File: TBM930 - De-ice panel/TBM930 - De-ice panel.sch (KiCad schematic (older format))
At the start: 21 parts, among them J1 Conn_01x02_Male, J2 Conn_01x02_Male, J3 Conn_01x02_Male, J4 Conn_01x02_Male, J5 Conn_01x02_Male, J6 Conn_01x02_Male, J7 Conn_01x02_Male, Q1 BS170, Q2 BS170, U1 ArduinoMEGA2560PROEmbed

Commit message: TBM930 updates
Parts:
- removed J1, J2, J3, J4, J5, J6, J7: Conn_01x02_Male, symbol Connector:Conn_01x02_Male
- added Q3: BS170, Package_TO_SOT_THT:TO-92_Inline, symbol Transistor_FET:BS170
- added R4: 10k, Resistor_SMD:R_1206_3216Metric_Pad1.30x1.75mm_HandSolder, symbol Device:R
- added SW1, SW2, SW3, SW4, SW5, SW6, SW7: SW_SPDT, Switches:MiniToggleSPDT terminal mount, symbol Switch:SW_SPDT
- D1, D2, D3, D4, D5: footprint (none) -> LED_THT:LED_D5.0mm
- D6, D7, D8: footprint (none) -> LED_SMD:LED_1206_3216Metric_Pad1.42x1.75mm_HandSolder
- R1, R2, R3: footprint (none) -> Resistor_SMD:R_1206_3216Metric_Pad1.30x1.75mm_HandSolder
- U1: footprint (none) -> Ardino:MEGA2560PROEmbed
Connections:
- net labels added: ANC_GND, LED_MASTER_GND, MASTER_POWER
- net labels removed: LED_GND
- wire segments 19 -> 37
- no-connect marks 62 -> 68
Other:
- note added: "Annunciators"
- note added: "Backlight"
- note added: "LED brightness control"
- note added: "Master LED power"
- note removed: "Annunciator LED brightness control"
- note removed: "Backlight LED brightness control"
- moved on the sheet: D1, D2, D3, D4, D5, D6, D7, D8, R1, R2, R3

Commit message: Switch to use the LED driver chip
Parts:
- removed D6, D7, D8: LED, LED_SMD:LED_1206_3216Metric_Pad1.42x1.75mm_HandSolder, symbol Device:LED
- removed Q1, Q2, Q3: BS170, Package_TO_SOT_THT:TO-92_Inline, symbol Transistor_FET:BS170
- removed SW1, SW2, SW3, SW4, SW5, SW6, SW7: SW_SPDT, Switches:MiniToggleSPDT terminal mount, symbol Switch:SW_SPDT
- added C1: 0.1uF, Capacitor_THT:C_Disc_D5.0mm_W2.5mm_P5.00mm, symbol Device:C
- added J1: SW_AIRFRAME_DE_ICE, Connector_Molex:Molex_KK-254_AE-6410-02A_1x02_P2.54mm_Vertical, symbol Connector:Conn_01x02_Male
- added J2: SW_ICE_LIGHT, Connector_Molex:Molex_KK-254_AE-6410-02A_1x02_P2.54mm_Vertical, symbol Connector:Conn_01x02_Male
- added J3: SW_PROP_DE_ICE, Connector_Molex:Molex_KK-254_AE-6410-02A_1x02_P2.54mm_Vertical, symbol Connector:Conn_01x02_Male
- added J4: SW_WIND_SHIELD, Connector_Molex:Molex_KK-254_AE-6410-02A_1x02_P2.54mm_Vertical, symbol Connector:Conn_01x02_Male
- added J5: SW_PITOT_L_HTR, Connector_Molex:Molex_KK-254_AE-6410-02A_1x02_P2.54mm_Vertical, symbol Connector:Conn_01x02_Male
- added J6: SW_PITOT_R_HTR, Connector_Molex:Molex_KK-254_AE-6410-02A_1x02_P2.54mm_Vertical, symbol Connector:Conn_01x02_Male
- added J7: SW_INERT_SEP, Connector_Molex:Molex_KK-254_AE-6410-02A_1x02_P2.54mm_Vertical, symbol Connector:Conn_01x02_Male
- added U2: TLC5916IN, Package_DIP:DIP-16_W7.62mm_Socket, symbol Mobiflight~docs:TLC5916IN
- D4: value WINDSHILED 1 -> WINDSHIELD 1
- R1: footprint Resistor_SMD:R_1206_3216Metric_Pad1.30x1.75mm_HandSolder -> Resistor_THT:R_Axial_DIN0207_L6.3mm_D2.5mm_P7.62mm_Horizontal
- R2, R3, R4: value 10k -> R; footprint Resistor_SMD:R_1206_3216Metric_Pad1.30x1.75mm_HandSolder -> Resistor_THT:R_Axial_DIN0207_L6.3mm_D2.5mm_P7.62mm_Horizontal
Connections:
- net labels added: +5V_LED, AIRFRAME_1, AIRFRAME_2, ANNUNCIATOR_CLOCK, ANNUNCIATOR_DATA, ANNUNCIATOR_LATCH, CURRENT_LIMITER, PROP, WINDSHIELD_1, WINDSHIELD_2
- net labels removed: AIRFRAME_1_LED, AIRFRAME_2_LED, ANC_GND, BACKLIGHT_BRIGHTNESS, BACKLIGHT_GND, LED_MASTER_GND, MASTER_POWER, PROP_LED, WINDSHIELD_1_LED, WINDSHIELD_2_LED
- wire segments 37 -> 23
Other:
- note added: "Switches are mounted to the board via the shaft\nand connected with Molex connectors so they can\nbe removed and re-used in other projects.\n"
- note removed: "Annunciators"
- note removed: "Backlight"
- note removed: "Backlight LEDs"
- note removed: "LED brightness control"
- note removed: "Master LED power"
- moved on the sheet: D1, D2, D3, D4, D5

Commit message: Create global library for footprints and symbols
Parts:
- removed R4: R, Resistor_THT:R_Axial_DIN0207_L6.3mm_D2.5mm_P7.62mm_Horizontal, symbol Device:R
- removed U1: ArduinoMEGA2560PROEmbed, Ardino:MEGA2560PROEmbed, symbol Arduino:ArduinoMEGA2560PROEmbed
- removed U2: TLC5916IN, Package_DIP:DIP-16_W7.62mm_Socket, symbol Mobiflight~docs:TLC5916IN
- added C2: 0.1uF, Capacitor_THT:C_Disc_D5.0mm_W2.5mm_P5.00mm, symbol Device:C
- added D10, D11, D12, D13, D14, D15, D16, D17, D18, D19, D20, D6, D7, D8, D9: LED, LED_SMD:LED_1206_3216Metric_Pad1.42x1.75mm_HandSolder, symbol Device:LED
- added J8: Barrel_Jack, Global MobiFlight panel parts:BarrelJack_Horizontal, symbol Connector:Barrel_Jack
- added SW1: SW_Push_Dual, symbol Switch:SW_Push_Dual
- added U1, U2: TLC5917IN, Package_DIP:DIP-16_W7.62mm, symbol Global_MobiFlight_panel_parts:TLC5917IN
- added U3: ArduinoMEGA2560PROEmbed, Ardino:MEGA2560PROEmbed, symbol Global_MobiFlight_panel_parts:ArduinoMEGA2560PROEmbed
- R2, R3: value R -> 1k
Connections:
- net labels added: +12V_LED, BACKLIGHT1, BACKLIGHT2, BACKLIGHT3, BACKLIGHT4, BACKLIGHT5, BACKLIGHT_BRIGHTNESS, BACKLIGHT_CLOCK, BACKLIGHT_DATA, BACKLIGHT_LATCH, LTS_TEST
- net labels removed: CURRENT_LIMITER
- wire segments 23 -> 35
- no-connect marks 68 -> 69
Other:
- note added: "12V LED power"
- note added: "Backlight LEDs"
- note added: "Light test"
- moved on the sheet: C1, D1, D2, D3, D4, D5, J1, J2, J3, J4, J5, J6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

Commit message: Massive de-ice panel update
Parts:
- removed D15: LED, LED_SMD:LED_1206_3216Metric_Pad1.42x1.75mm_HandSolder, symbol Device:LED
- removed SW1: SW_Push_Dual, symbol Switch:SW_Push_Dual
- removed U2: TLC5917IN, Package_DIP:DIP-16_W7.62mm, symbol Global_MobiFlight_panel_parts:TLC5917IN
- added D20, D21, D22: LED, LED_SMD:LED_1206_3216Metric_Pad1.42x1.75mm_HandSolder, symbol Device:LED
- added SW1: SW_Push, Button_Switch_THT:SW_PUSH_6mm_H9.5mm, symbol Switch:SW_Push
- added U3: TLC5917IN, Package_DIP:DIP-16_W7.62mm, symbol Global_MobiFlight_panel_parts:TLC5917IN
- U1: renamed from U3; footprint Ardino:MEGA2560PROEmbed -> Global MobiFlight panel parts:MEGA2560PROEmbed
- renumbered D16 to D15, D17 to D16, D18 to D17, D19 to D18, D20 to D19, U1 to U2
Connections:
- net labels added: BACKLIGHT6, LED_CLOCK, LED_DATA, LED_LATCH
- net labels removed: ANNUNCIATOR_CLOCK, ANNUNCIATOR_DATA, ANNUNCIATOR_LATCH, BACKLIGHT_CLOCK, BACKLIGHT_DATA, BACKLIGHT_LATCH
- wire segments 35 -> 32
- no-connect marks 69 -> 68
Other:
- moved on the sheet: D14, J8, R2

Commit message: Routed!
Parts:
- added D23, D24: LED, LED_SMD:LED_1206_3216Metric_Pad1.42x1.75mm_HandSolder, symbol Device:LED
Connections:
- net labels added: BACKLIGHT7
- wire segments 32 -> 34
- no-connect marks 68 -> 67
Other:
- moved on the sheet: C1, C2, D1, D10, D11, D12, D13, D14, D15, D16, D17, D18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

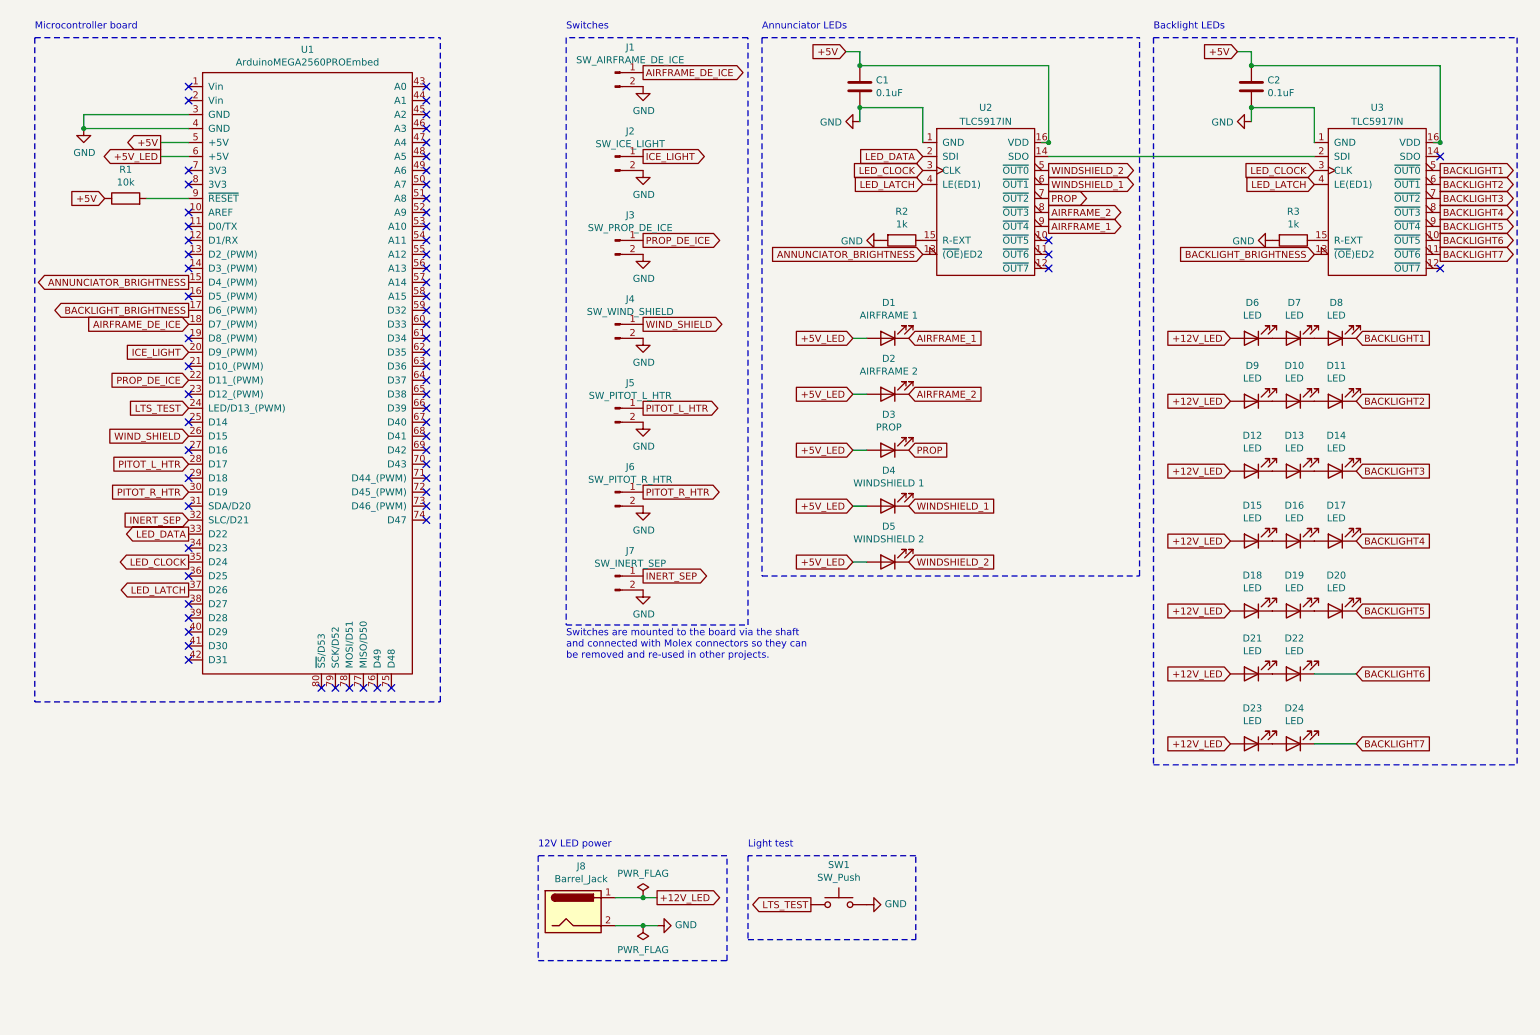
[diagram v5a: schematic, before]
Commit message: Switch to smaller Arduino
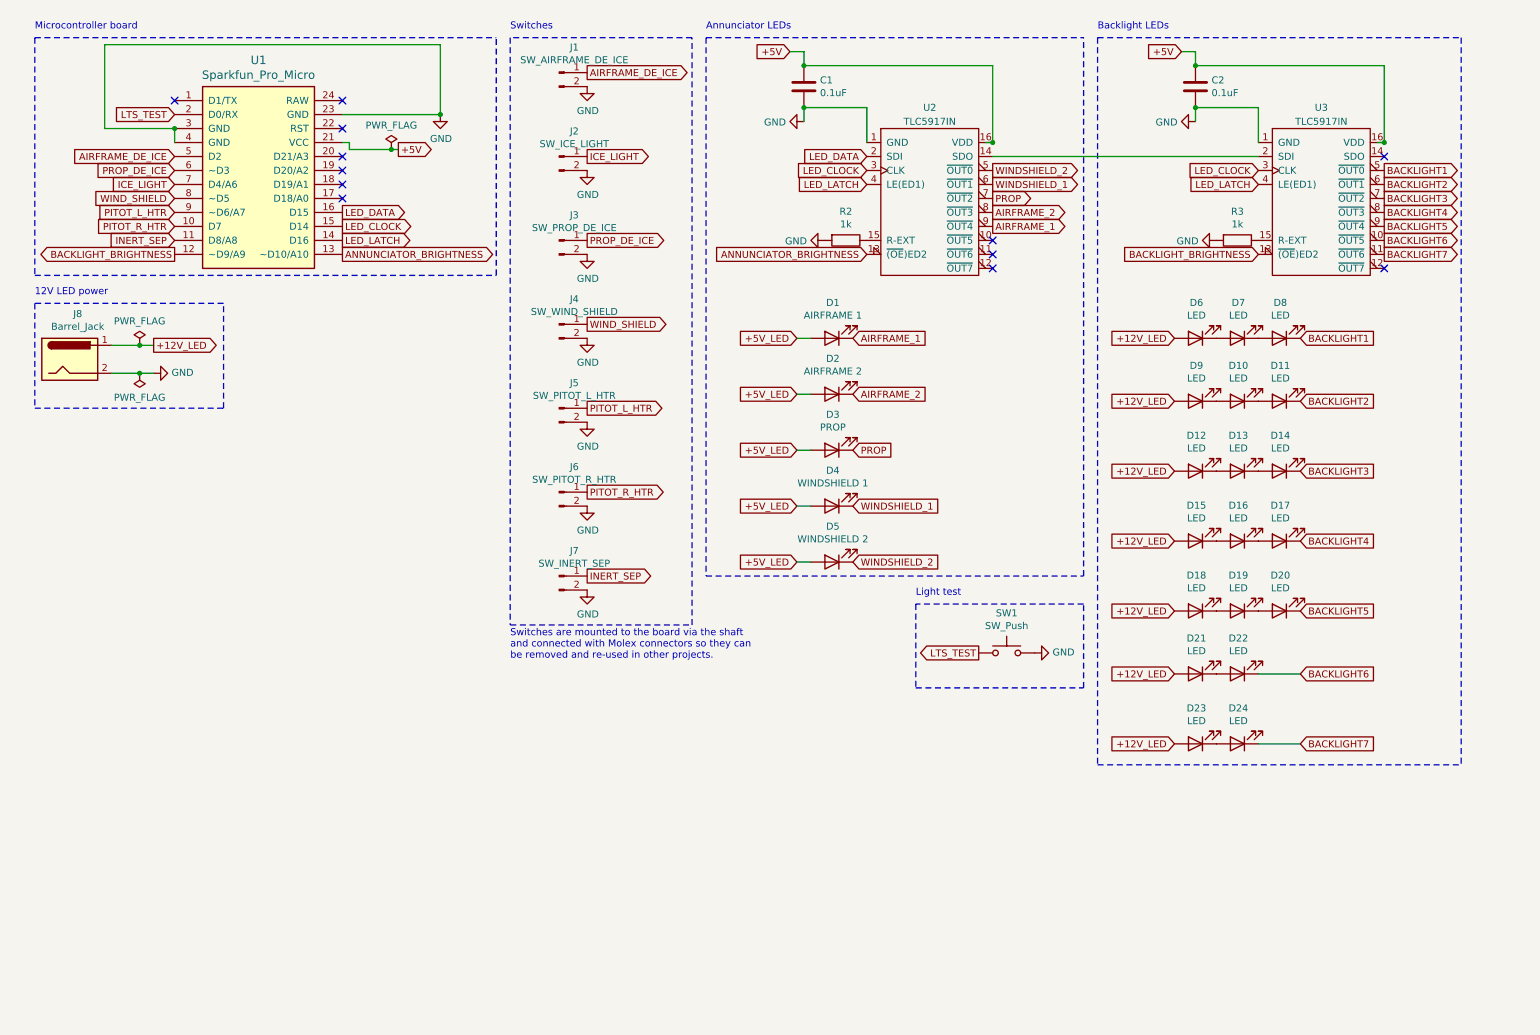
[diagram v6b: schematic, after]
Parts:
- removed R1: 10k, Resistor_THT:R_Axial_DIN0207_L6.3mm_D2.5mm_P7.62mm_Horizontal, symbol Device:R
- removed U1: ArduinoMEGA2560PROEmbed, Global MobiFlight panel parts:MEGA2560PROEmbed, symbol Global_MobiFlight_panel_parts:ArduinoMEGA2560PROEmbed
- added U1: Sparkfun_Pro_Micro, Arduino:Sparkfun_Pro_Micro, symbol Arduino:Sparkfun_Pro_Micro
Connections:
- wire segments 34 -> 38
- no-connect marks 67 -> 12
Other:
- moved on the sheet: C1, C2, D1, D10, D11, D12, D13, D14, D15, D16, D17, D18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

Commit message: Microcontroller righton the board
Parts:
- removed U1: Sparkfun_Pro_Micro, Arduino:Sparkfun_Pro_Micro, symbol Arduino:Sparkfun_Pro_Micro
- added C10, C9: 20pF, symbol Device:C
- added C11, C14, C8: 0.1uF, symbol Device:C
- added C12, C6: 10uF, symbol Device:CP
- added C13, C3, C4, C5, C7: 1uF, symbol Device:C
- added D25, D27, D28: LED, symbol Device:LED
- added FB1: 500mA, symbol Device:Ferrite_Bead
- added FB2: Ferrite_Bead, symbol Device:Ferrite_Bead
- added J10: AVR-ISP-6, symbol Connector:AVR-ISP-6
- added J9: USB_B_Micro, symbol Connector:USB_B_Micro
- added NT1: Net-Tie_2, symbol Device:Net-Tie_2
- added R1, R4: 330, symbol Device:R
- added R5: 1K, symbol Device:R
- added R6, R7: 22, symbol Device:R
- added R8: 10K, symbol Device:R
- added SW2: SW_Push, symbol Switch:SW_Push
- added U1: ATmega16U4-MU-Exposed-Extra-Pins, Package_DFN_QFN:QFN-44-1EP_7x7mm_P0.5mm_EP5.2x5.2mm, symbol Global_MobiFlight_panel_parts:ATmega16U4-MU-Exposed-Extra-Pins
- added Y1: 16MHz, symbol Device:Crystal
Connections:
- net labels added: A0, A1, A2, A3, A4, A5, BACKLIGHT_BRIGHT, D+, D-, D10, D12, D13, D17, D2, D3, D4, D5, D6, D7, D8, D9, INDICATOR_BRIGHT, MISO, MOSI, RXI, SCK, TXO, XTAL1, XTAL2, ~RESET
- net labels removed: +5V_LED, ANNUNCIATOR_BRIGHTNESS, BACKLIGHT_BRIGHTNESS
- wire segments 38 -> 115
- no-connect marks 12 -> 13
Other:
- note added: "AVR-ISP programing interface"
- note added: "Microcontroller"
- note added: "Oscillator"
- note added: "USB and +5V power"
- note removed: "Microcontroller board"
- moved on the sheet: C1, C2, D1, D10, D11, D12, D13, D14, D15, D16, D17, D18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

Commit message: Placed components on PCB, working on routing
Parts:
- removed FB1: 500mA, symbol Device:Ferrite_Bead
- C1: renamed from C3; footprint (none) -> Capacitor_SMD:C_0603_1608Metric; JLC (none) -> 0603; LCSC (none) -> C15849
- C10: renamed from C12; footprint (none) -> Capacitor_SMD:C_0603_1608Metric; JLC (none) -> 0603; LCSC (none) -> C15850
- C11: renamed from C13; footprint (none) -> Capacitor_SMD:C_0603_1608Metric; JLC (none) -> 0603; LCSC (none) -> C15849
- C12: renamed from C14; footprint (none) -> Capacitor_SMD:C_0603_1608Metric; JLC (none) -> 0603; LCSC (none) -> C14663
- C13: renamed from C1; footprint Capacitor_THT:C_Disc_D5.0mm_W2.5mm_P5.00mm -> Capacitor_SMD:C_0603_1608Metric; JLC (none) -> 0603; LCSC (none) -> C14663
- C14: renamed from C2; footprint Capacitor_THT:C_Disc_D5.0mm_W2.5mm_P5.00mm -> Capacitor_SMD:C_0603_1608Metric; JLC (none) -> 0603; LCSC (none) -> C14663
- C2: renamed from C4; footprint (none) -> Capacitor_SMD:C_0603_1608Metric; JLC (none) -> 0603; LCSC (none) -> C15849
- C3: renamed from C9; footprint (none) -> Capacitor_SMD:C_0603_1608Metric; JLC (none) -> 0603; LCSC (none) -> C1648
- C4: renamed from C10; footprint (none) -> Capacitor_SMD:C_0603_1608Metric; JLC (none) -> 0603; LCSC (none) -> C1648
- C5: renamed from C6; footprint (none) -> Capacitor_SMD:C_0603_1608Metric; JLC (none) -> 0603; LCSC (none) -> C15850
- C6: renamed from C7; footprint (none) -> Capacitor_SMD:C_0603_1608Metric; JLC (none) -> 0603; LCSC (none) -> C15849
- C7: renamed from C8; footprint (none) -> Capacitor_SMD:C_0603_1608Metric; JLC (none) -> 0603; LCSC (none) -> C14663
- C8: renamed from C5; footprint (none) -> Capacitor_SMD:C_0603_1608Metric; JLC (none) -> 0603; LCSC (none) -> C15849
- C9: renamed from C11; footprint (none) -> Capacitor_SMD:C_0603_1608Metric; JLC (none) -> 0603; LCSC (none) -> C14663
- D1: renamed from D27; footprint (none) -> LED_SMD:LED_0603_1608Metric; JLC (none) -> LED_0603; LCSC (none) -> C2290
- D10: renamed from D9; footprint LED_SMD:LED_1206_3216Metric_Pad1.42x1.75mm_HandSolder -> LED_SMD:LED_0603_1608Metric; JLC (none) -> LED_0603; LCSC (none) -> C2290
- D11: renamed from D12; footprint LED_SMD:LED_1206_3216Metric_Pad1.42x1.75mm_HandSolder -> LED_SMD:LED_0603_1608Metric; JLC (none) -> LED_0603; LCSC (none) -> C2290
- D12: renamed from D15; footprint LED_SMD:LED_1206_3216Metric_Pad1.42x1.75mm_HandSolder -> LED_SMD:LED_0603_1608Metric; JLC (none) -> LED_0603; LCSC (none) -> C2290
- D13: renamed from D18; footprint LED_SMD:LED_1206_3216Metric_Pad1.42x1.75mm_HandSolder -> LED_SMD:LED_0603_1608Metric; JLC (none) -> LED_0603; LCSC (none) -> C2290
- D14: renamed from D21; footprint LED_SMD:LED_1206_3216Metric_Pad1.42x1.75mm_HandSolder -> LED_SMD:LED_0603_1608Metric; JLC (none) -> LED_0603; LCSC (none) -> C2290
- D15: renamed from D23; footprint LED_SMD:LED_1206_3216Metric_Pad1.42x1.75mm_HandSolder -> LED_SMD:LED_0603_1608Metric; JLC (none) -> LED_0603; LCSC (none) -> C2290
- D16: renamed from D7; footprint LED_SMD:LED_1206_3216Metric_Pad1.42x1.75mm_HandSolder -> LED_SMD:LED_0603_1608Metric; JLC (none) -> LED_0603; LCSC (none) -> C2290
- D17: renamed from D10; footprint LED_SMD:LED_1206_3216Metric_Pad1.42x1.75mm_HandSolder -> LED_SMD:LED_0603_1608Metric; JLC (none) -> LED_0603; LCSC (none) -> C2290
- D18: renamed from D13; footprint LED_SMD:LED_1206_3216Metric_Pad1.42x1.75mm_HandSolder -> LED_SMD:LED_0603_1608Metric; JLC (none) -> LED_0603; LCSC (none) -> C2290
- D19: renamed from D16; footprint LED_SMD:LED_1206_3216Metric_Pad1.42x1.75mm_HandSolder -> LED_SMD:LED_0603_1608Metric; JLC (none) -> LED_0603; LCSC (none) -> C2290
- D2: renamed from D28; footprint (none) -> LED_SMD:LED_0603_1608Metric; JLC (none) -> LED_0603; LCSC (none) -> C2290
- D20: renamed from D19; footprint LED_SMD:LED_1206_3216Metric_Pad1.42x1.75mm_HandSolder -> LED_SMD:LED_0603_1608Metric; JLC (none) -> LED_0603; LCSC (none) -> C2290
- D21: renamed from D22; footprint LED_SMD:LED_1206_3216Metric_Pad1.42x1.75mm_HandSolder -> LED_SMD:LED_0603_1608Metric; JLC (none) -> LED_0603; LCSC (none) -> C2290
- D22: renamed from D24; footprint LED_SMD:LED_1206_3216Metric_Pad1.42x1.75mm_HandSolder -> LED_SMD:LED_0603_1608Metric; JLC (none) -> LED_0603; LCSC (none) -> C2290
- D23: renamed from D8; footprint LED_SMD:LED_1206_3216Metric_Pad1.42x1.75mm_HandSolder -> LED_SMD:LED_0603_1608Metric; JLC (none) -> LED_0603; LCSC (none) -> C2290
- D24: renamed from D11; footprint LED_SMD:LED_1206_3216Metric_Pad1.42x1.75mm_HandSolder -> LED_SMD:LED_0603_1608Metric; JLC (none) -> LED_0603; LCSC (none) -> C2290
- D25: renamed from D14; footprint LED_SMD:LED_1206_3216Metric_Pad1.42x1.75mm_HandSolder -> LED_SMD:LED_0603_1608Metric; JLC (none) -> LED_0603; LCSC (none) -> C2290
- D26: renamed from D17; footprint LED_SMD:LED_1206_3216Metric_Pad1.42x1.75mm_HandSolder -> LED_SMD:LED_0603_1608Metric; JLC (none) -> LED_0603; LCSC (none) -> C2290
- D27: renamed from D20; footprint LED_SMD:LED_1206_3216Metric_Pad1.42x1.75mm_HandSolder -> LED_SMD:LED_0603_1608Metric; JLC (none) -> LED_0603; LCSC (none) -> C2290
- D3: renamed from D25; footprint (none) -> LED_SMD:LED_0603_1608Metric; JLC (none) -> LED_0603; LCSC (none) -> C2290
- D4: renamed from D1; JLC (none) -> SMD-CRY-3225_4P; LCSC (none) -> C13738
- D9: renamed from D6; footprint LED_SMD:LED_1206_3216Metric_Pad1.42x1.75mm_HandSolder -> LED_SMD:LED_0603_1608Metric; JLC (none) -> LED_0603; LCSC (none) -> C2290
- FB1: renamed from FB2; footprint (none) -> Resistor_SMD:R_0805_2012Metric; JLC (none) -> 0805; LCSC (none) -> C1017
- J1: renamed from J9; footprint (none) -> Connector_USB:USB_Micro-B_Molex-105017-0001
- J10: footprint (none) -> Connector_PinHeader_1.00mm:PinHeader_1x06_P1.00mm_Vertical
- NT1: footprint (none) -> NetTie:NetTie-2_SMD_Pad0.5mm
- R1: renamed from R8; footprint (none) -> Resistor_SMD:R_0603_1608Metric; JLC (none) -> 0603; LCSC (none) -> C25804
- R2: renamed from R6; footprint (none) -> Resistor_SMD:R_0603_1608Metric; JLC (none) -> 0603; LCSC (none) -> C23345
- R3: renamed from R7; footprint (none) -> Resistor_SMD:R_0603_1608Metric; JLC (none) -> 0603; LCSC (none) -> C23345
- R4: renamed from R5; footprint (none) -> Resistor_SMD:R_0603_1608Metric; JLC (none) -> 0603; LCSC (none) -> C21190
- R5: renamed from R1; footprint (none) -> Resistor_SMD:R_0603_1608Metric; JLC (none) -> 0603; LCSC (none) -> C23138
- R6: renamed from R4; footprint (none) -> Resistor_SMD:R_0603_1608Metric; JLC (none) -> 0603; LCSC (none) -> C23138
- R7: renamed from R2; footprint Resistor_THT:R_Axial_DIN0207_L6.3mm_D2.5mm_P7.62mm_Horizontal -> Resistor_SMD:R_0603_1608Metric; JLC (none) -> 0603; LCSC (none) -> C21190
- R8: renamed from R3; footprint Resistor_THT:R_Axial_DIN0207_L6.3mm_D2.5mm_P7.62mm_Horizontal -> Resistor_SMD:R_0603_1608Metric; JLC (none) -> 0603; LCSC (none) -> C21190
- SW1: renamed from SW2; footprint (none) -> Button_Switch_THT:SW_PUSH_6mm_H4.3mm; JLC (none) -> 0603
- SW2: renamed from SW1; JLC (none) -> 0603
- Y1: footprint (none) -> Crystal:Crystal_SMD_3225-4Pin_3.2x2.5mm; JLC (none) -> SMD-CRY-3225_4P; LCSC (none) -> C13738
- renumbered D2 to D5, D3 to D6, D4 to D7, D5 to D8, J8 to J2, J1 to J3, J2 to J4, J3 to J5, J4 to J6, J5 to J7, J6 to J8, J7 to J9
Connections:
- net labels added: +12V, SW_AIRFRAME, SW_ICE_LIGHT, SW_INERT_SEP, SW_LTS_TEST, SW_PITOT_L, SW_PITOT_R, SW_PROP, SW_WINDSHIELD
- net labels removed: AIRFRAME_DE_ICE, ICE_LIGHT, INERT_SEP, LTS_TEST, PITOT_L_HTR, PITOT_R_HTR, PROP_DE_ICE, WIND_SHIELD
- wire segments 115 -> 114
